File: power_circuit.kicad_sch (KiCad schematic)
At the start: 0 parts

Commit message: Update power circuit schematic
* Start implementing power circuit design with MOSFET gate driver and
  pulse signal transformer section.
* Project file is updated since the libraries used in the schematic
  have changed.
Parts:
- added C201, C203, C205: C, symbol Device:C
- added C202, C204: C_Polarized, symbol Device:C_Polarized
- added D201, D202: 1N4148, Diode_THT:D_DO-35_SOD27_P7.62mm_Horizontal, symbol Diode:1N4148
- added D203, D204: BZV55C5V1, Diode_SMD:D_MiniMELF, symbol Diode:BZV55C5V1
- added J201, J202: Screw_Terminal_01x01, TerminalBlock_MetzConnect:TerminalBlock_MetzConnect_360271_1x01_Horizontal_ScrewM3.0_Boxed, symbol Connector:Screw_Terminal_01x01
- added R201, R202, R203, R204, R205, R206, R207, R208: R, symbol Device:R
- added T201: 2,8 mH / 1,714:1:1, symbol probable-chemical-burns:750342744
- added T202, T204: T-BJT-NPN, symbol PCM_Elektuur_1:T-BJT-NPN
- added T203, T205: T-BJT-PNP, symbol PCM_Elektuur_1:T-BJT-PNP
- added U201: UCC27324x, probable-chemical-burns:SOIC127P599X175-8N, symbol probable-chemical-burns:UCC27324x
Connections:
- new net: D201.1 (K), R205.1
- new net: D203.1 (K), R205.2, R206.2, U201.2 (IN_{A})
- new net: R201.1, R202.2, T204.2 (B), T205.2 (B)
- new net: R201.2, T201.7, T204.3 (E), T205.3 (E)
- new net: R203.2, R204.1, T202.2 (B), T203.2 (B)
- new net: R204.2, T201.6, T202.3 (E), T203.3 (E)
- new net: D201.2 (A), T201.1
- new net: D202.1 (K), R207.1
- new net: D204.1 (K), R207.2, R208.1, U201.4 (IN_{B})
- new net: U201.1 (N/A), U201.8 (N/A)
- new net: D202.2 (A), T201.3
- new net +12V: C201.1, C202.1, U201.6 (V_{DD})
- new net GND: C201.2, C202.2, D203.2 (A), D204.2 (A), R206.1, R208.2, T201.2, T201.4, U201.3 (G_{ND})
- new net GNDPWR: C203.2, C204.2, C205.2, J202.1 (Pin_1), T203.1 (C), T205.1 (C)
- new net HG: U201.7 (OUTA)
- new net LG: U201.5 (OUTB)
- new net SHG: R203.1
- new net SLG: R202.1
- new net VCC: C203.1, C204.1, C205.1, J201.1 (Pin_1), T202.1 (C), T204.1 (C)

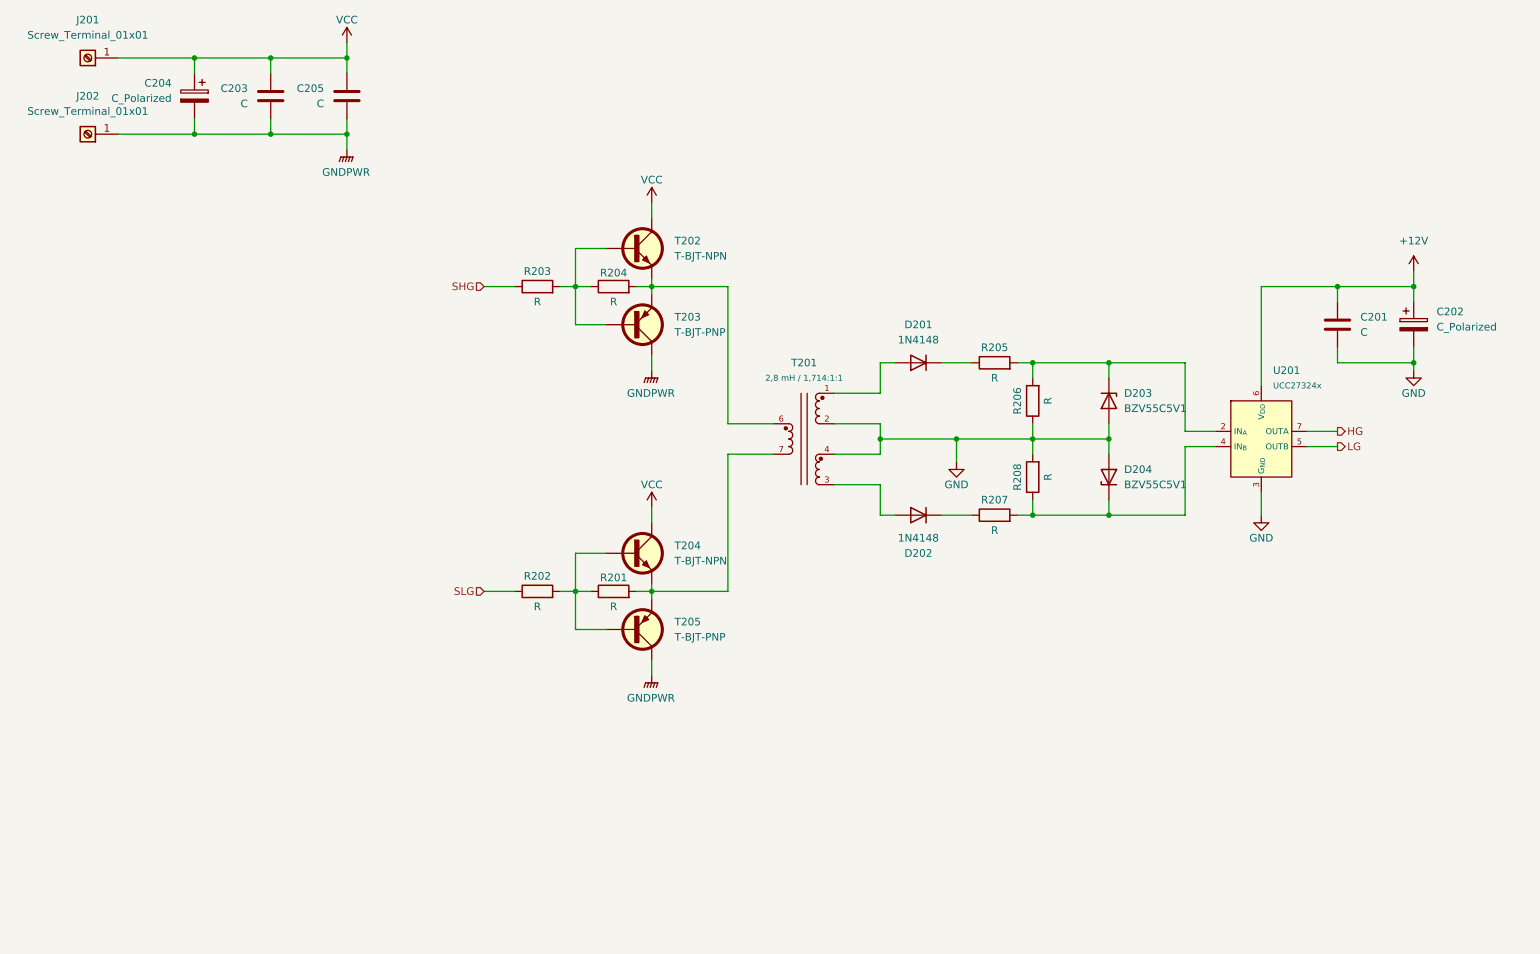
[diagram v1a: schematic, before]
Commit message: [WIP] Update power circuit schematic
* Update MOSFET driver/buffer to new symbol.
* Update passive components values.
* Implement photomultiplier.

NOTE :
  This is work in progress and shall be amended or merged when work on
  this file is complete.
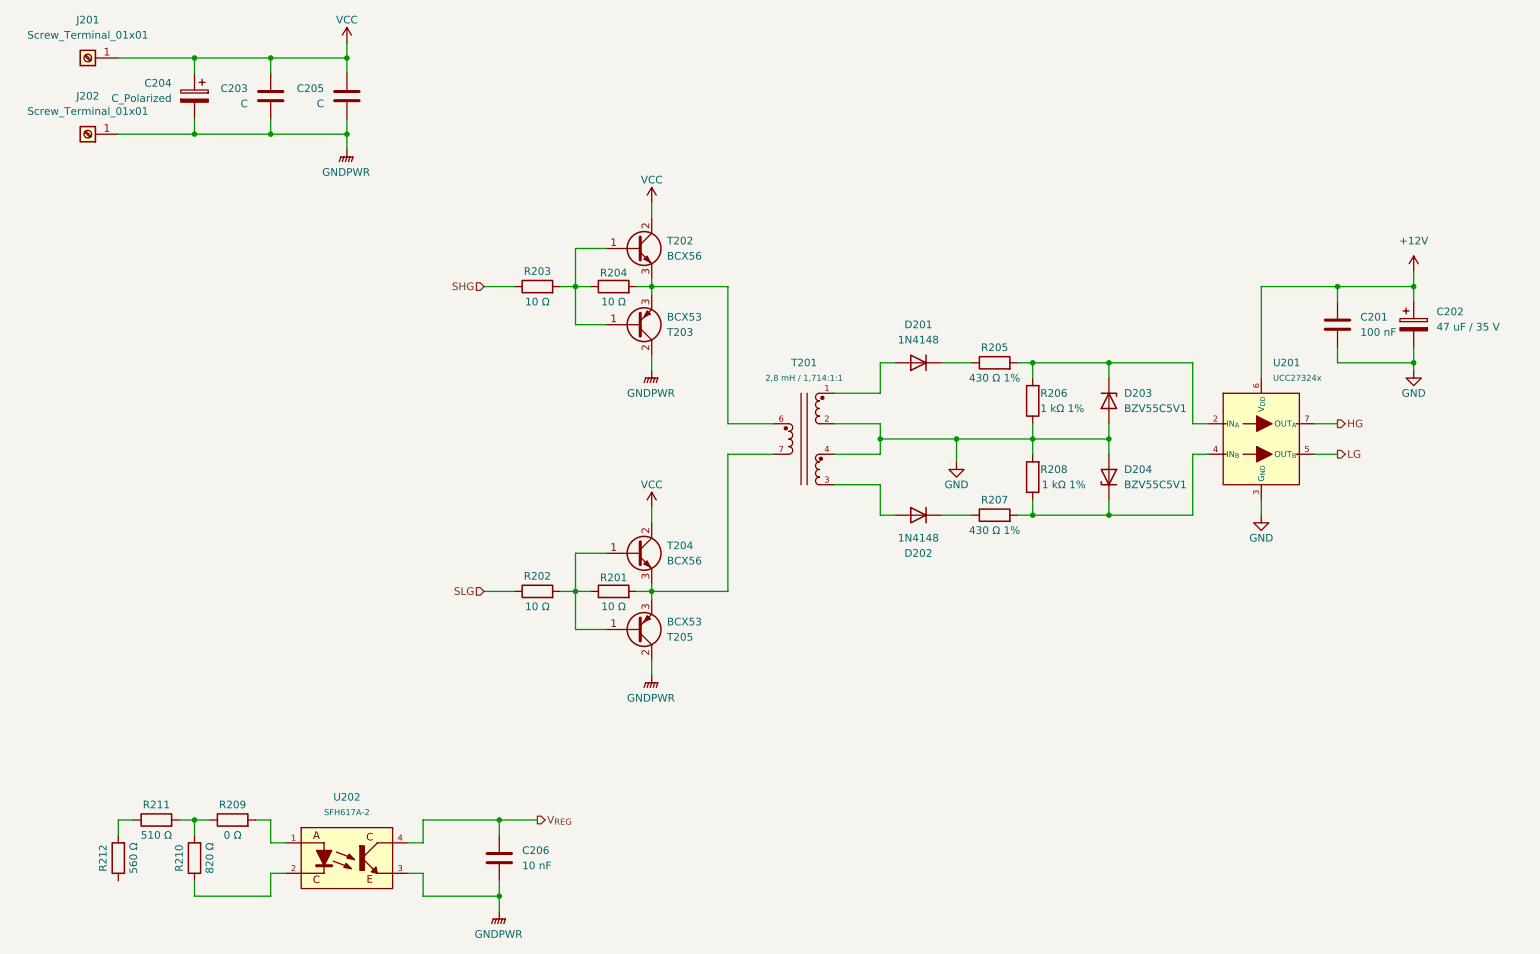
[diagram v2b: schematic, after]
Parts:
- added C206: 10 nF, symbol Device:C
- added R209: 0 Ω, symbol Device:R
- added R210: 820 Ω, symbol Device:R
- added R211: 510 Ω, symbol Device:R
- added R212: 560 Ω, symbol Device:R
- added U202: SFH617A-2, probable-chemical-burns:DIP762W50P254L458H480Q4, symbol probable-chemical-burns:SFH617A-2
- C201: value C -> 100 nF
- C202: value C_Polarized -> 47 uF / 35 V
- R201, R202, R203, R204: value R -> 10 Ω
- R205, R207: value R -> 430 Ω 1%
- R206, R208: value R -> 1 kΩ 1%
- T202, T204: value T-BJT-NPN -> BCX56; footprint (none) -> Package_TO_SOT_SMD:SOT-89-3; symbol PCM_Elektuur_1:T-BJT-NPN -> Transistor_BJT:BCX56
- T203, T205: value T-BJT-PNP -> BCX53; footprint (none) -> Package_TO_SOT_SMD:SOT-89-3; symbol PCM_Elektuur_1:T-BJT-PNP -> Transistor_BJT:BCX53
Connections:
- net GNDPWR: now also T203.2 (C), T205.2 (C), C206.2, U202.3 (E); no longer T203.1 (C), T205.1 (C)
- net VCC: now also T202.2 (C), T204.2 (C); no longer T202.1 (C), T204.1 (C)
- net at R201.1, R202.2: now also T204.1 (B), T205.1 (B); no longer T204.2 (B), T205.2 (B)
- net at R203.2, R204.1: now also T202.1 (B), T203.1 (B); no longer T202.2 (B), T203.2 (B)
- new net: R210.1, U202.2 (K)
- new net: R209.1, R210.2, R211.2
- new net: R211.1, R212.2
- new net: R209.2, U202.1 (A)
- new net V_{REG}: C206.1, U202.4 (C)
